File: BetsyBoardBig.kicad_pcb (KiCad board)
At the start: 4 copper layers, 50 x 50 mm, 59 parts, among them J1 CLOCKS, J2 SPI, J3 USB_B_Micro, J4 USART1, J5 I2C, J6 USART3, J7 ANALOG, J8 Micro_SD_Card, P1 BATT, P2 CORTEX-JTAG, SW1 JUMPER, SW2 TE-FSM4J, SW3 SW_PUSH_NO_ALT, U1 TLV75733PDBVR‎, U2 USBLC6-2SC6, U3 74LVC3G14, U4 STM32L486Rx-LQFP64, U5 74LVC1G3157, U6 IS25WP256D-xM, X1 XTAL, Y1 Crystal

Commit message: Prepare for second run.
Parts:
- removed J4: USART1, Connector_PinHeader_2.54mm:PinHeader_1x03_P2.54mm_Horizontal
- added J9: USART1, Connector_PinHeader_2.54mm:PinHeader_1x04_P2.54mm_Horizontal, F.Cu at (140.9, 69.3)
- added R8: 5K1, Resistor_SMD:R_0603_1608Metric, F.Cu at (134.2, 91.1)
- added R9: 5K1, Resistor_SMD:R_0603_1608Metric, F.Cu at (127.5, 89.4)
- added TP2-BOOT1: TestPoint_Probe, engstad:pin-socket-1, F.Cu at (137.8, 65.5)
- J3: value USB_B_Micro -> USB_C_Receptacle_USB2.0; footprint engstad:usb-micro-b-amphenol-fci-10118194-oval -> Connector_USB:USB_C_Receptacle_GCT_USB4085
- TP1-NRST1: renamed from TP1-RST#1; footprint engstad:test-point-smd-5016 -> engstad:pin-socket-1
- TP2-BOOT0: footprint engstad:test-point-smd-5016 -> engstad:pin-socket-1
- moved TP1-NRST1 8.41 mm to (137.8, 62.9)
- moved TP2-BOOT0 6.59 mm to (137.8, 60.4)
- moved J3 5.66 mm to (128.2, 93.9)
- moved C14 3.65 mm to (137.7, 77.5), turned to 270 degrees
- moved D1 1.41 mm to (125.8, 89.4)
- moved D2 1.41 mm to (124.2, 89.4)
- moved R7 1.38 mm to (124.2, 92.5)
- moved P2 1.35 mm to (133.6, 74.2)
- moved U2 1.20 mm to (131.2, 90.7)
- moved C13 1.17 mm to (124.8, 87.1), turned to 0 degrees
- moved SW3 0.95 mm to (131.6, 83.0)
- moved R6 0.79 mm to (126.5, 91.8), turned to 0 degrees
- moved FB1 0.47 mm to (122.4, 91.5)
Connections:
- net /LED_RED renamed /USR_LED
- P2 pad 10: (no net) -> /~JTRST
- U2 pad 1: /OTGFS_D+ -> /D+
- U2 pad 3: /OTGFS_D- -> /D-
- U2 pad 4: /D- -> /ID-
- U2 pad 6: /D+ -> /ID+
- U4 pad 44: /OTGFS_D- -> /D-
- U4 pad 45: /OTGFS_D+ -> /D+
- U4 pad 61: /USR_BTN -> (no net)
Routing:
- net /USR_BTN: track 38.7 -> 16.7 mm, vias 4 -> 2
- net /OTGFS_D-: track 18.0 -> 0.00 mm
- net /OTGFS_D+: track 18.0 -> 0.00 mm
- net Net-(J3-PadS1): track 0.00 -> 15.4 mm
- net /D+: track 3.07 -> 17.1 mm
- net /D-: track 3.09 -> 17.1 mm
- net Net-(J3-Pad6): track 11.6 -> 0.00 mm
- net /SDMMC_DET: track 30.4 -> 20.1 mm
- net /CC2: track 0.00 -> 8.07 mm, vias 0 -> 1
- net VCC: track 68.0 -> 75.1 mm, vias 19 -> 20
- net /~JTRST: track 0.00 -> 7.02 mm
- net /VBUS: track 16.8 -> 23.6 mm
- net /BOOT0: track 32.7 -> 26.8 mm, vias 1 -> 0
- net /CC1: track 0.00 -> 5.34 mm, vias 0 -> 1
- net /ID-: track 0.00 -> 4.50 mm, vias 0 -> 1
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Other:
- board text added: "PA2"
- board text added: "PA8"
- board text added: "PB2"
- board text added: "PC13"

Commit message: Use 4-pin QSPI NOR Flash card
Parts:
- U6: value IS25WP256D-xM -> IS25LP06D-xB; footprint Package_SO:SOIC-16W_7.5x10.3mm_P1.27mm -> Package_SO:SOIC-8_5.275x5.275mm_P1.27mm
- moved C20 13.1 mm to (111.6, 80.5), turned to 180 degrees
- moved U6 3.70 mm to (110.3, 84.4)
- moved C17 0.85 mm to (111.6, 78.8), turned to 180 degrees
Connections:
- J3 pad A8: (no net) -> Net-(J3-PadA8)
- J3 pad B8: (no net) -> Net-(J3-PadB8)
- P2 pad 7: (no net) -> Net-(P2-Pad7)
- U1 pad 4: (no net) -> Net-(U1-Pad4)
- U4 pad 61: (no net) -> Net-(U4-Pad61)
- U6 pad 1: /QSPI_IO3 -> /QSPI_CS#
- U6 pad 2: VCC -> /QSPI_IO1
- U6 pad 3: (no net) -> /QSPI_IO2
- U6 pad 4: (no net) -> GND
- U6 pad 5: (no net) -> /QSPI_IO0
- U6 pad 6: (no net) -> /QSPI_SCK
- U6 pad 7: /QSPI_CS# -> /QSPI_IO3
- U6 pad 8: /QSPI_IO1 -> VCC
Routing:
- net /QSPI_CS#: track 26.7 -> 12.5 mm
- net /QSPI_IO0: track 26.7 -> 13.5 mm, vias 2 -> 0
- net /QSPI_IO1: track 26.7 -> 14.2 mm
- net /QSPI_IO2: track 26.8 -> 16.3 mm, vias 0 -> 2
- net VCC: track 75.1 -> 65.2 mm
- net GND: track 104.3 -> 113.3 mm, vias 40 -> 39
- net /USART3_RTS: track 18.4 -> 16.8 mm
- net /QSPI_SCK: track 12.0 -> 10.8 mm, vias 2 -> 0
- net /RTC_OUT: track 32.0 -> 31.5 mm
- net /QSPI_IO3: vias 0 -> 2

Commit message: Latest work on big version
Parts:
- removed FB1: 220Ω@100MHz, Inductor_SMD:L_0805_2012Metric
- removed TP2-BOOT1: TestPoint_Probe, engstad:pin-socket-1
- added B1: BATT, engstad:Battery_Keystone_2894, B.Cu at (126.5, 61.3)
- added C21: 1uF, Capacitor_SMD:C_0805_2012Metric, F.Cu at (122.9, 91.3)
- added C22: 1uF, Capacitor_SMD:C_0805_2012Metric, F.Cu at (121.7, 87.4)
- added D3: B130LAW, Diode_SMD:D_SOD-123, F.Cu at (108.0, 90.6)
- added F1: Polyfuse, Fuse:Fuse_0805_2012Metric, F.Cu at (124.9, 91.3)
- added Q1: FDN340P, Package_TO_SOT_SMD:SOT-23, F.Cu at (111.0, 91.3)
- added R10: 1K, Resistor_SMD:R_0603_1608Metric, F.Cu at (119.2, 88.3)
- added R11: 100K, Resistor_SMD:R_0603_1608Metric, F.Cu at (124.3, 88.7)
- added TP3: TestPoint_Probe, engstad:pin-socket-1, F.Cu at (136.8, 65.5)
- added U7: MCP73831-2-OT, Package_TO_SOT_SMD:SOT-23-5, F.Cu at (120.0, 91.1)
- C12: value 10uF -> 1uF; footprint Capacitor_SMD:C_0805_2012Metric -> Capacitor_SMD:C_0603_1608Metric
- R3: value 100K -> 1M
- TP1: renamed from TP1-NRST1; footprint engstad:pin-socket-1 -> TestPoint:TestPoint_Pad_1.0x1.0mm; moved to F.Cu
- TP2: renamed from TP2-BOOT0; footprint engstad:pin-socket-1 -> TestPoint:TestPoint_Pad_1.0x1.0mm; moved to F.Cu
- moved P1 47.6 mm to (100.5, 89.2), turned to 180 degrees
- moved R7 41.0 mm to (135.8, 53.1), turned to 90 degrees
- moved D2 37.6 mm to (134.1, 53.1), turned to 270 degrees
- moved TP2 12.0 mm to (129.8, 69.3)
- moved TP1 7.75 mm to (130.4, 65.3)
- moved SW1 6.54 mm to (131.0, 52.8), turned to 270 degrees
- moved C3 5.02 mm to (117.2, 91.3), turned to 90 degrees
- moved U1 4.89 mm to (114.7, 91.2)
- moved C4 3.98 mm to (114.8, 88.2), turned to 0 degrees
- moved R5 3.52 mm to (125.1, 86.4), turned to 270 degrees
- moved D1 3.12 mm to (126.7, 86.4)
- moved R2 2.98 mm to (128.6, 59.2), turned to 90 degrees
- moved J7 2.83 mm to (100.1, 83.2)
- moved R1 2.29 mm to (131.8, 59.2), turned to 90 degrees
- moved R4 2.28 mm to (121.1, 84.9), turned to 180 degrees
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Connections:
- J3 pad A4: /VBUS -> /VBUS_IN
- J3 pad A9: /VBUS -> /VBUS_IN
- J3 pad B4: /VBUS -> /VBUS_IN
- J3 pad B9: /VBUS -> /VBUS_IN
- P1 pad 1: /VBAT_IN -> /VBAT
- TP2 pad 1: /BOOT0 -> /~JTRST
- U4 pad 61: Net-(U4-Pad61) -> /PB8
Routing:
- net GND: track 113.3 -> 66.3 mm, vias 39 -> 21
- net VCC: track 65.2 -> 37.6 mm, vias 20 -> 10
- net /USR_BTN: track 16.7 -> 0.00 mm, vias 2 -> 0
- net /SPI2_CIPO: track 30.4 -> 13.7 mm, vias 2 -> 1
- net /SPI2_CS#: track 29.7 -> 13.8 mm
- net Net-(J3-PadS1): track 15.4 -> 0.00 mm
- net /USART3_CTS: track 17.6 -> 2.52 mm
- net /OPAMP_OUT: track 17.1 -> 2.12 mm
- net /DAC_OUT2: track 19.5 -> 4.58 mm
- net /PB8: track 0.00 -> 14.3 mm, vias 0 -> 1
- net /USART3_RXD: track 24.1 -> 10.7 mm
- net /SPI2_COPI: track 27.8 -> 14.4 mm, vias 2 -> 1
- net /USART3_TXD: track 24.5 -> 11.2 mm
- net /USR_LED: track 14.7 -> 1.67 mm
- net /VBAT_IN: track 5.09 -> 16.4 mm, vias 0 -> 1
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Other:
- board size 50 x 50 mm -> 48 x 48 mm
- board text added: "ASW"
- board text removed: "BOOT0"
- board text removed: "~RST~"

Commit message: Getting ready for "final" big version.
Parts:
- added D4: RED, LED_SMD:LED_0603_1608Metric, F.Cu at (104.6, 85.9)
- added R12: 1K, Resistor_SMD:R_0603_1608Metric, F.Cu at (129.7, 74.0)
- D1: value RED -> BLUE
- J7: footprint Connector_PinHeader_2.54mm:PinHeader_1x10_P2.54mm_Horizontal -> Connector_PinHeader_2.54mm:PinHeader_2x06_P2.54mm_Horizontal
- R4: value 10K -> 470
- R5: value 1K -> 10K
- R7: value 180 -> 1K
- moved R7 36.2 mm to (121.7, 86.4)
- moved D2 35.0 mm to (123.3, 86.4), turned to 90 degrees
- moved C22 19.2 mm to (102.5, 86.0)
- moved R4 16.2 mm to (105.3, 88.3), turned to 0 degrees
- moved R5 16.1 mm to (129.7, 71.0)
- moved U7 14.7 mm to (105.3, 91.1)
- moved C13 13.2 mm to (128.0, 74.0), turned to 90 degrees
- moved R10 10.9 mm to (108.8, 92.0)
- moved C4 5.60 mm to (120.2, 89.7), turned to 270 degrees
- moved TP2 5.52 mm to (133.7, 65.4)
- moved J7 4.62 mm to (102.6, 79.4)
- moved D3 3.95 mm to (112.0, 90.5)
- moved C3 3.33 mm to (114.2, 89.8), turned to 270 degrees
- moved P1 3.15 mm to (98.2, 87.0), turned to 90 degrees
- moved Q1 2.90 mm to (109.0, 89.3), turned to 180 degrees
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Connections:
- net /USR_BTN renamed Net-(R12-Pad2)
- net /VBAT_IN renamed /COIN+
- C2 pad 1: /VBAT -> /VCOIN
- C22 pad 1: /VBAT -> /VBATT
- J7 pad 1: VSSA -> VDDA
- J7 pad 10: VDDA -> /COMP_IN-
- J7 pad 2: /DAC_OUT2 -> VDDA
- J7 pad 3: /DAC_OUT1 -> VSSA
- J7 pad 4: /COMP_OUT -> VSSA
- J7 pad 5: /COMP_IN+ -> /DAC_OUT1
- J7 pad 6: /COMP_IN- -> /DAC_OUT2
- J7 pad 7: /OPAMP_OUT -> /COMP_IN+
- J7 pad 8: /OPAMP_IN+ -> /COMP_OUT
- J7 pad 9: /OPAMP_IN- -> /OPAMP_OUT
- P1 pad 1: /VBAT -> /VBATT
- Q1 pad 3: /VBAT -> /VBATT
- R4 pad 1: VCC -> Net-(D4-Pad1)
- R4 pad 2: /USR_SW -> /STAT
- R5 pad 1: /USR_SW -> VCC
- SW1 pad 2: /VBAT -> /VCOIN
- U4 pad 1: /VBAT -> /VCOIN
- U7 pad 1: Net-(U7-Pad1) -> /STAT
- U7 pad 3: /VBAT -> /VBATT
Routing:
- net GND: track 66.3 -> 106.2 mm, vias 21 -> 54
- net /VBAT: track 24.9 -> 0.00 mm, vias 2 -> 0
- net /USR_SW: track 2.12 -> 25.3 mm, vias 0 -> 2
- net /VCOIN: track 0.00 -> 22.9 mm, vias 0 -> 2
- net Net-(R12-Pad2): track 0.00 -> 18.4 mm, vias 0 -> 2
- net /VIN: track 0.00 -> 17.4 mm
- net Net-(J3-PadS1): track 0.00 -> 15.4 mm
- net /COIN+: track 16.4 -> 31.7 mm, vias 1 -> 2
- net /SPI2_CIPO: track 13.7 -> 28.8 mm, vias 1 -> 2
- net /VBUS: track 24.3 -> 11.5 mm, vias 0 -> 6
- net /USART3_TXD: track 11.2 -> 23.8 mm
- net /USART3_RXD: track 10.7 -> 23.2 mm
- net /USART3_CTS: track 2.52 -> 15.0 mm
- net /SPI2_COPI: track 14.4 -> 26.7 mm, vias 1 -> 2
- net /DAC_OUT2: track 4.58 -> 15.7 mm
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- added copper zone on F.Cu, net /VBATT
- added copper zone on Pow.Cu, net /VBATT
- added copper zone on F.Cu, net /VBUS
- added copper zone on F.Cu, net GND
- added copper zone on F.Cu, net VCC
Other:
- board text added: "VBUS"
- board text removed: "3.3"
- board text removed: "5.0"
- board text removed: "A1"
- board text removed: "A2"
- board text removed: "CI+"
- board text removed: "CI-"
- board text removed: "CO"
- board text removed: "OP+"
- board text removed: "OP-"
- board text removed: "OPO"
- board text removed: "PWR"
- board text removed: "USR"

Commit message: Save from old computer.
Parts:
- added TP4: TestPoint_Probe, TestPoint:TestPoint_Pad_1.0x1.0mm, F.Cu at (130.4, 65.3)
- moved TP2 3.72 mm to (136.8, 67.5)
- moved TP1 2.05 mm to (128.4, 65.3)
- turned B1 to 180 degrees
- turned R12 to -90 degrees
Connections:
- net /~JTRST renamed /~{JTRST}
- net /~MR renamed /~{MR}
- net /~RST renamed /~{RST}
- J3 pad A8: Net-(J3-PadA8) -> unconnected-(J3-PadA8)
- J3 pad B8: Net-(J3-PadB8) -> unconnected-(J3-PadB8)
- J3 pad S1: Net-(J3-PadS1) -> unconnected-(J3-PadS1)
- P2 pad 7: Net-(P2-Pad7) -> unconnected-(P2-Pad7)
- R12 pad 2: Net-(R12-Pad2) -> /SW3
- R5 pad 2: Net-(R12-Pad2) -> /USR_SW
- SW3 pad 2: Net-(R12-Pad2) -> /SW3
- U1 pad 4: Net-(U1-Pad4) -> unconnected-(U1-Pad4)
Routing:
- net /VBUS: track 11.5 -> 35.5 mm, vias 6 -> 0
- net Net-(R12-Pad2): track 18.4 -> 0.00 mm, vias 2 -> 0
- net unconnected-(J3-PadS1): track 0.00 -> 15.4 mm
- net Net-(J3-PadS1): track 15.4 -> 0.00 mm
- net /SW3: track 0.00 -> 13.0 mm, vias 0 -> 2
- net /USR_SW: track 25.3 -> 18.5 mm
- net /QSPI_SCK: track 10.8 -> 14.9 mm
- net /~{JTRST}: track 1.87 -> 5.16 mm
- net /~{RST}: track 17.5 -> 18.6 mm
- net /BOOT0: track 26.3 -> 27.3 mm
- net /SPI2_SCK: track 37.0 -> 37.8 mm
- net GND: track 106.2 -> 106.7 mm
- net /PB8: track 17.4 -> 16.9 mm
- net /SDMMC_D2: track 24.3 -> 23.8 mm
- added copper zone on In2.Cu, net /VBATT
- added copper zone on In1.Cu, net GND
- added copper zone on In2.Cu, net VCC
- added copper zone on In2.Cu, net VDDA
- added copper zone on In1.Cu, net VSSA
- removed copper zone on Pow.Cu, net /VBATT
- removed copper zone on Gnd.Cu, net GND
- removed copper zone on Pow.Cu, net VCC
- removed copper zone on Pow.Cu, net VDDA
- removed copper zone on Gnd.Cu, net VSSA
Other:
- net class Default removed
- net class PowerMain removed
- net class USB removed
- board text added: "PA1/PA0"
- board text added: "PA2/PB7"
- board text added: "PA4/PA5"
- board text added: "PB6/PB5"
- board text added: "PC4"
- board text added: "PC5"
- board text added: "RESET/ BOOT"
- board text removed: "BOOT"
- board text removed: "OCLK_LS"
- board text removed: "OCLK_M"
- board text removed: "PA0/ADC5"
- board text removed: "PA1/ADC6"
- board text removed: "PA3/ADC8"
- board text removed: "PA4/ADC9"
- board text removed: "PA5/ADC10"
- board text removed: "PB5"
- board text removed: "PB6"
- board text removed: "PB7"
- board text removed: "PC4/CMP1_IN-/A13"
- board text removed: "PC5/CMP1_IN-/A14"
- board text removed: "RTC_OUT"
- board text removed: "RTC_TS"
- board text removed: "VBUS (5V)"
- board text removed: "VCC (3.3V)"

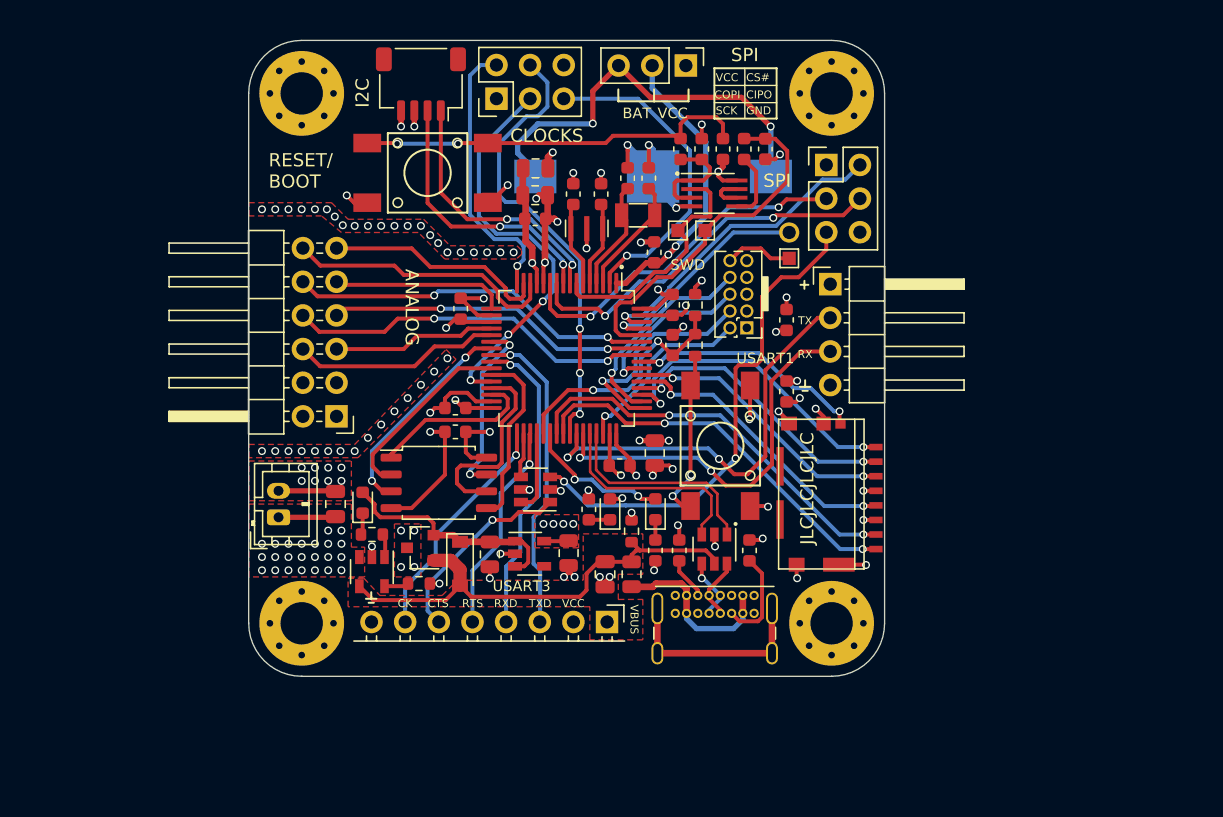
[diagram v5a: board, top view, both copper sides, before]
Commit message: More work on battery charging.
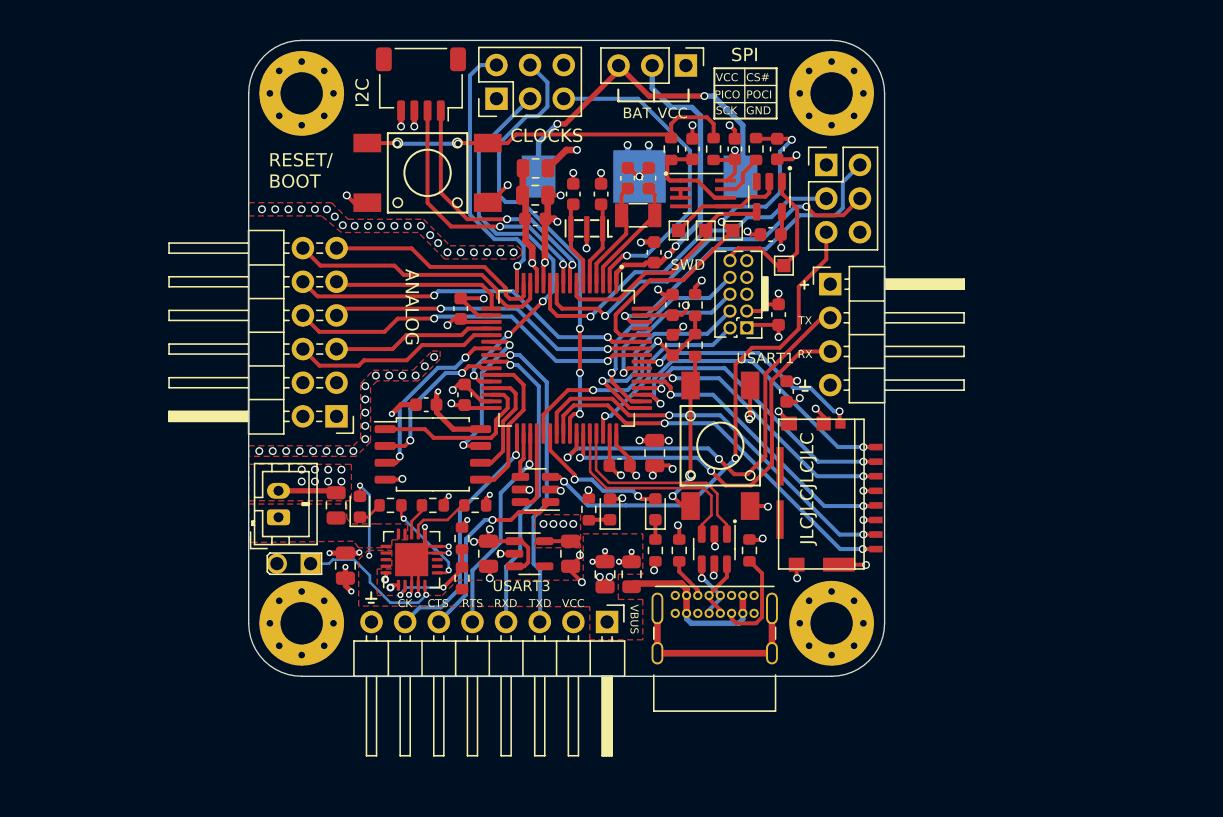
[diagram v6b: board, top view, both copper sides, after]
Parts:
- removed D4: RED, LED_SMD:LED_0603_1608Metric
- removed Q1: FDN340P, Package_TO_SOT_SMD:SOT-23
- removed the TP3 at (136.8, 65.5)
- removed the U7 at (105.3, 91.1)
- added C24: 0.1uF, Capacitor_SMD:C_0603_1608Metric, F.Cu at (132.7, 59.2)
- added C25: 0.1uF, Capacitor_SMD:C_0603_1608Metric, F.Cu at (135.4, 65.7)
- added C7: 4.7uF, Capacitor_SMD:C_0805_2012Metric, F.Cu at (102.6, 86.1)
- added P2: BATT, engstad:pin-socket-2, F.Cu at (99.4, 90.5)
- added R1: 330K, Resistor_SMD:R_0603_1608Metric, F.Cu at (112.1, 91.6)
- added R2: 110K, Resistor_SMD:R_0603_1608Metric, F.Cu at (112.1, 88.6)
- added TP2: TestPoint_Probe, TestPoint:TestPoint_Pad_1.0x1.0mm, F.Cu at (128.4, 65.3)
- added U3: MCP73871, Package_DFN_QFN:QFN-20-1EP_4x4mm_P0.5mm_EP2.5x2.5mm, F.Cu at (108.3, 90.2)
- added U4: 74LVC1G08, Package_TO_SOT_SMD:SOT-23-5, F.Cu at (135.3, 62.8)
- B1: footprint engstad:Battery_Keystone_2894 -> Engstad:Battery_Keystone_2894
- C1: renamed from C21; value 1uF -> 10uF
- C4: renamed from C22; value 1uF -> 4.7uF
- D1: renamed from D3; value B130LAW -> RED; footprint Diode_SMD:D_SOD-123 -> LED_SMD:LED_0603_1608Metric
- J8: footprint engstad:Molex_PS_105162_001 -> Engstad:Molex_PS_105162_001
- R12: renamed from R4; value 470 -> 330
- R14: renamed from R7; value 1K -> 330
- R5: renamed from R11; value 100K -> 10K
- R6: renamed from R10; value 1K -> 100K
- SW2, SW3: footprint engstad:TACTILE_SWITCH-TE-FSM4JSMAATR -> Engstad:TACTILE_SWITCH-TE-FSM4JSMAATR
- moved R5 15.1 mm to (109.9, 86.1), turned to 180 degrees
- moved D1 8.69 mm to (104.4, 86.2), turned to 90 degrees
- moved R6 7.27 mm to (113.1, 86.1)
- moved C4 4.71 mm to (103.3, 90.7)
- moved C23 3.01 mm to (109.4, 78.5)
- moved R12 2.61 mm to (106.7, 86.1)
- moved U8 2.20 mm to (109.9, 82.2)
- moved TP4 2.10 mm to (132.6, 65.3)
- moved TP1 2.10 mm to (130.5, 65.3)
- moved C19 1.22 mm to (112.3, 77.8), turned to 90 degrees
- moved B1 1.03 mm to (125.5, 61.3)
- moved C11 0.90 mm to (135.9, 59.2)
- moved R9 0.90 mm to (134.3, 59.2)
- moved U5 0.85 mm to (130.3, 62.5)
- moved C9 0.72 mm to (136.0, 71.7)
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- renumbered C11 to C10, C12 to C11, C7 to C12, C8 to C13, C9 to C14, C10 to C15, C13 to C16, C15 to C17, C16 to C18, C17 to C19, C5 to C2, C18 to C20, C19 to C21, C14 to C22, C20 to C23, C6 to C3, C3 to C5, C4 to C6, C2 to C8, C1 to C9, D1 to D2, D2 to D3, FB2 to FB1, J3 to J1, J1 to J2, J2 to J3, J5 to J4, J6 to J5, J7 to J6, J9 to J7, P2 to P3, R5 to R10, R12 to R11, R6 to R13, R8 to R3, R9 to R4, R1 to R7, R2 to R8, R3 to R9, TP2 to TP3, U3 to U5, U4 to U6, U5 to U7, U6 to U8
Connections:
- net /SPI2_CIPO renamed /SPI2_POCI
- net /SPI2_COPI renamed /SPI2_PICO
- net Net-(R1-Pad2) renamed /SW
- C1 pad 1: /VBUS -> VBUS
- C4 pad 1: /VBATT -> /VIN
- D1 pad 1: /VIN -> Net-(D1-K)
- D1 pad 2: /VBUS -> VBUS
- F1 pad 1: /VBUS -> VBUS
- J5 pad 1: /VBUS -> VBUS
- P1 pad 1: /VBATT -> /V_BAT
- R12 pad 1: Net-(D4-Pad1) -> Net-(D1-K)
- R12 pad 2: /STAT -> /~{PG}
- R5 pad 2: /VBUS -> /PRG1
- R6 pad 2: /PRG -> /PRG3
- R9 pad 2: Net-(R3-Pad2) -> /BOOT_{M}
- U2 pad 5: /VBUS -> VBUS
- U5 pad 2: /~{RST} -> /RST_{M}
- U5 pad 3: /~{MR} -> /RST_{M}
- U5 pad 5: Net-(R3-Pad2) -> /~{RST_{M}}
- U5 pad 6: Net-(U3-Pad6) -> /~{MR}
- U5 pad 7: Net-(U3-Pad6) -> /BOOT_{M}
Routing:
- net /VBUS: track 35.5 -> 0.00 mm
- net VCC: track 44.0 -> 65.5 mm, vias 20 -> 21
- net /PB8: track 16.9 -> 0.00 mm, vias 1 -> 0
- net /THM: track 0.00 -> 11.5 mm, vias 0 -> 1
- net VBUS: track 0.00 -> 10.8 mm, vias 0 -> 7
- net /~{RST_{M}}: track 0.00 -> 8.87 mm
- net /VPCC: track 0.00 -> 8.00 mm, vias 0 -> 2
- net /~{PG}: track 0.00 -> 7.45 mm, vias 0 -> 2
- net /~{JTRST}: track 5.16 -> 12.4 mm
- net /VIN: track 17.4 -> 10.8 mm, vias 0 -> 6
- net /QSPI_SCK: track 14.9 -> 8.80 mm
- net /COIN+: track 31.7 -> 26.4 mm
- net Net-(R3-Pad2): track 5.17 -> 0.00 mm
- net GND: track 106.7 -> 101.9 mm, vias 54 -> 64
- net /PRG3: track 0.00 -> 4.76 mm
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- added copper zone on In2.Cu, net /VIN
- added copper zone on F.Cu, net /V_BAT
- added copper zone on F.Cu, net VBUS
- added copper zone on In2.Cu, net VBUS
- removed copper zone on F.Cu, net /VBATT
- removed copper zone on In2.Cu, net /VBATT
- removed copper zone on F.Cu, net /VBUS
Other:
- board text added: "BetsyBoard v0.98 Engstad Design"
- board text added: "GND_{A}"
- board text added: "New"
- board text added: "PICO"
- board text added: "POCI"
- board text added: "THM"
- board text added: "VCC_{A}"
- board text added: "V_{BAT}"
- board text removed: "AGND"
- board text removed: "CIPO"
- board text removed: "COPI"
- board text removed: "VCCA"
